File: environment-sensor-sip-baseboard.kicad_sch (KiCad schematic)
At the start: 59 parts, among them J1 USB-C_GCT_USB4105-GF-A, J2 JST_SH_1x4_SM04B-SRSS-TB-LF-SN, J3 JST_SH_1x4_SM04B-SRSS-TB-LF-SN, U1 Myra-231F1F08, U5 SHT45, U6 BME280

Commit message: [#62396] Fix ERC and DRC
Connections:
- net GND: now also U1.B1 (MP), U1.C1 (MP)

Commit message: [#62396] Update title block
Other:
- title: SiP Baseboard -> MYRA SiP Baseboard
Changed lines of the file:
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@@
   (paper "A3")
   (title_block
-    (title "SiP Baseboard")
+    (title "MYRA SiP Baseboard")
     (date "2024-06-28")
     (rev "1.0.0")

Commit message: [#62396] Update SiP
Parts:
- U1: GitHub (none) -> https://github.com/antmicro/myra-sip
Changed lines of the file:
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@@
     (title "MYRA SiP Baseboard")
     (date "2024-06-28")
-    (rev "1.0.0")
+    (rev "1.0.0:c359f")
     (company "Antmicro ")
     (comment 1 "www.antmicro.com")
@@
       (effects (font (size 1.27 1.27)) (justify left bottom) hide)
     )
+    (property "GitHub" "https://github.com/antmicro/myra-sip " (at 260.35 69.215 0)
+      (effects (font (size 1.27 1.27)) (justify left bottom) hide)
+    )

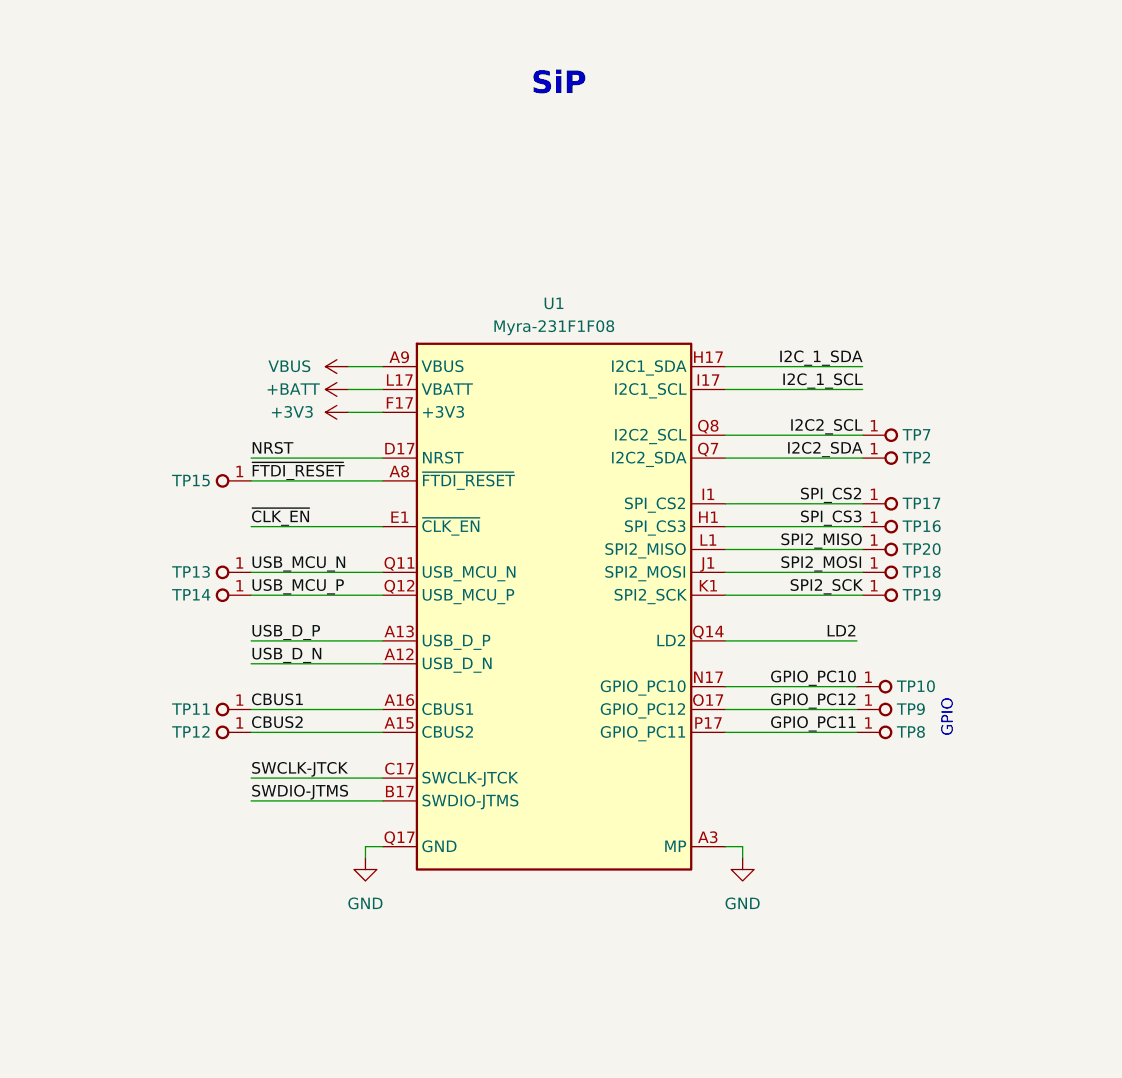
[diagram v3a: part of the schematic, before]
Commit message: [#62396] Update visualization
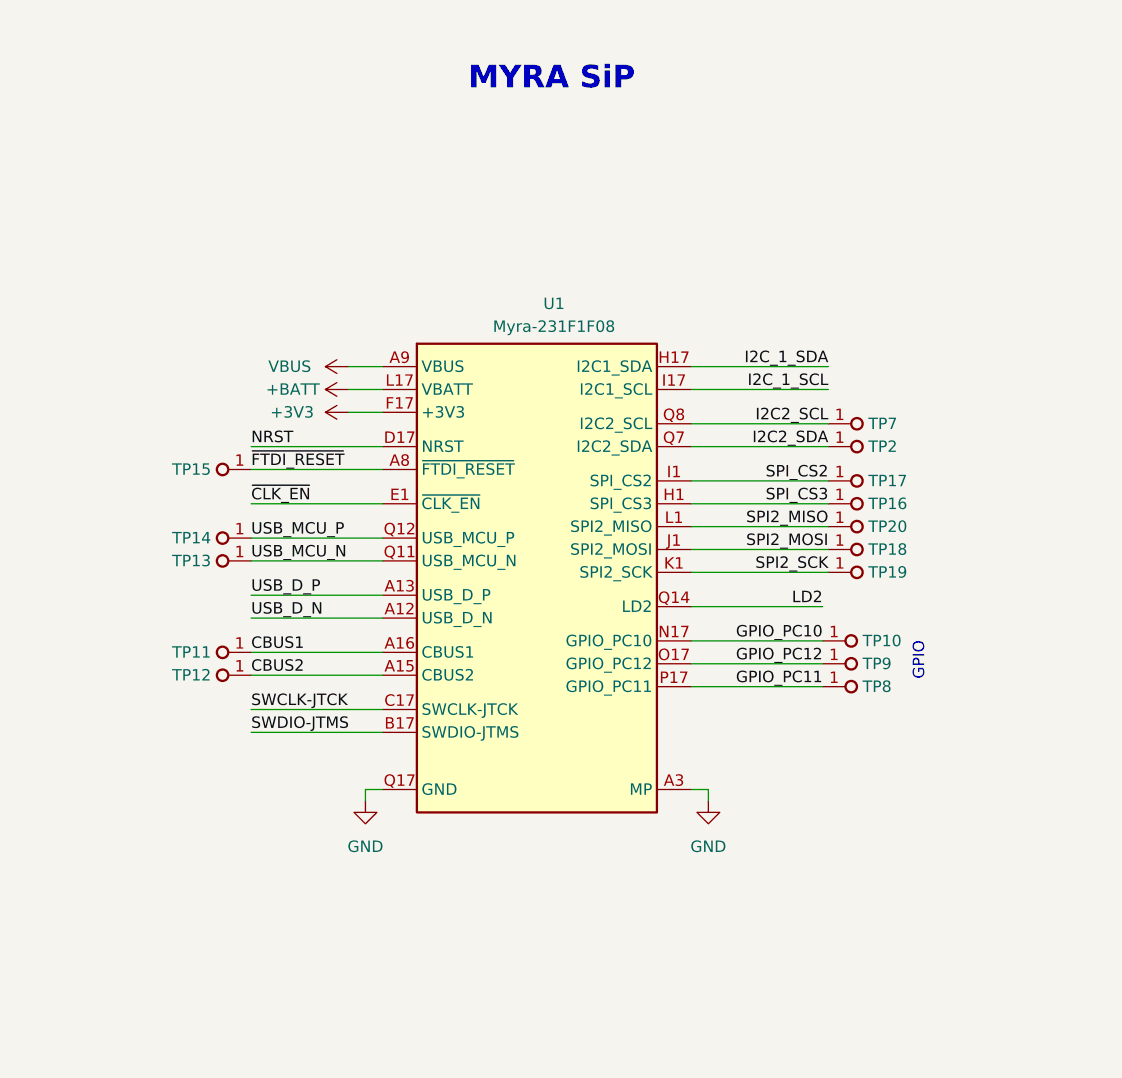
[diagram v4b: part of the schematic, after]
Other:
- note added: "MYRA SiP"
- note removed: "SiP"
- moved on the sheet: TP10, TP11, TP12, TP13, TP14, TP15, TP16, TP17, TP18, TP19, TP2, TP20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
